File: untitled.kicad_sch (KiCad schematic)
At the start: 3 parts, among them U3 ATmega328P-P, U4 ATmega328P-P, U5 ATmega328P-P

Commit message: kicad to Jeremy
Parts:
- added Q1: NMOS, symbol Simulation_SPICE:NMOS
- added R1: 200R, symbol Device:R
- added R2: 1K, symbol Device:R
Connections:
- new net: Q1.2 (G), R1.2, R2.2
- new net GPIO_Moteur: R2.1
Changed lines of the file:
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@@
 (kicad_sch (version 20230121) (generator eeschema)
   (paper "A4")
+  (junction (at 157.48 44.45) (diameter 0) (color 0 0 0 0)
+  )
   (wire (pts (xy 163.83 86.36) (xy 170.18 86.36))
     (stroke (width 0) (type default))
   )
+  (wire (pts (xy 157.48 59.69) (xy 157.48 44.45))
+    (stroke (width 0) (type default))
+  )
+  (wire (pts (xy 157.48 44.45) (xy 161.29 44.45))
+    (stroke (width 0) (type default))
+  )
+  (wire (pts (xy 157.48 44.45) (xy 154.94 44.45))
+    (stroke (width 0) (type default))
+  )
   (wire (pts (xy 83.82 86.36) (xy 90.17 86.36))
     (stroke (width 0) (type default))
   )
+  (wire (pts (xy 158.75 59.69) (xy 157.48 59.69))
+    (stroke (width 0) (type default))
+  )
   (wire (pts (xy 83.82 88.9) (xy 90.17 88.9))
     (stroke (width 0) (type default))
@@
     (stroke (width 0) (type default))
   )
+  (wire (pts (xy 142.24 44.45) (xy 147.32 44.45))
+    (stroke (width 0) (type default))
+  )
   (wire (pts (xy 236.22 88.9) (xy 242.57 88.9))
     (stroke (width 0) (type default))
@@
     (property "Intersheetrefs" "${INTERSHEET_REFS}" (at 101.7239 88.9 0)
       (effects (font (size 1.27 1.27)) (justify left) hide)
+    )
+  )
+  (global_label "GPIO_Moteur" (shape input) (at 142.24 44.45 180) (fields_autoplaced)
+    (effects (font (size 1.27 1.27)) (justify right))
+    (property "Intersheetrefs" "${INTERSHEET_REFS}" (at 127.5414 44.45 0)
+      (effects (font (size 1.27 1.27)) (justify right) hide)
     )
   )
@@
         )
       )
+    )
+  )
+  (symbol (lib_id "Device:R") (at 151.13 44.45 90) (unit 1)
+    (in_bom yes) (on_board yes) (dnp no) (fields_autoplaced)
+    (property "Reference" "R2" (at 151.13 38.1 90)
+      (effects (font (size 1.27 1.27)))
+    )
+    (property "Value" "1K" (at 151.13 40.64 90)
+      (effects (font (size 1.27 1.27)))
+    )
+    (property "Footprint" "" (at 151.13 46.228 90)
+      (effects (font (size 1.27 1.27)) hide)
+    )
+    (property "Datasheet" "~" (at 151.13 44.45 0)
+      (effects (font (size 1.27 1.27)) hide)
+    )
+    (pin "1")
+    (pin "2")
+    (instances
+      (project "MaisonEtape1"
+        (path "/ed06f8de-d1bb-4b1a-bfe3-5df11d3a9162/0600536b-f413-4b06-98e9-b5748b5de992"
+          (reference "R2") (unit 1)
+        )
+      )
+    )
+  )
+  (symbol (lib_id "Simulation_SPICE:NMOS") (at 166.37 44.45 0) (unit 1)
+    (in_bom yes) (on_board yes) (dnp no) (fields_autoplaced)
+    (property "Reference" "Q1" (at 172.72 43.18 0)
+      (effects (font (size 1.27 1.27)) (justify left))
+    )
+    (property "Value" "NMOS" (at 172.72 45.72 0)
+      (effects (font (size 1.27 1.27)) (justify left))
+    )
+    (property "Footprint" "" (at 171.45 41.91 0)
+      (effects (font (size 1.27 1.27)) hide)
+    )
+    (property "Datasheet" "https://ngspice.sourceforge.io/docs/ngspice-manual.pdf" (at 166.37 57.15 0)
+      (effects (font (size 1.27 1.27)) hide)
+    )
+    (property "Sim.Device" "NMOS" (at 166.37 61.595 0)
+      (effects (font (size 1.27 1.27)) hide)
+    )
+    (property "Sim.Type" "VDMOS" (at 166.37 63.5 0)
+      (effects (font (size 1.27 1.27)) hide)
+    )
+    (property "Sim.Pins" "1=D 2=G 3=S" (at 166.37 59.69 0)
+      (effects (font (size 1.27 1.27)) hide)
+    )
+    (pin "1")
+    (pin "2")
+    (pin "3")
+    (instances
+      (project "MaisonEtape1"
+        (path "/ed06f8de-d1bb-4b1a-bfe3-5df11d3a9162/0600536b-f413-4b06-98e9-b5748b5de992"
+          (reference "Q1") (unit 1)
+        )
+      )
+    )
+  )
+  (symbol (lib_id "Device:R") (at 162.56 59.69 270) (unit 1)
+    (in_bom yes) (on_board yes) (dnp no) (fields_autoplaced)
+    (property "Reference" "R1" (at 162.56 53.34 90)
+      (effects (font (size 1.27 1.27)))
+    )
+    (property "Value" "200R" (at 162.56 55.88 90)
+      (effects (font (size 1.27 1.27)))
+    )
+    (property "Footprint" "" (at 162.56 57.912 90)
+      (effects (font (size 1.27 1.27)) hide)
+    )
+    (property "Datasheet" "~" (at 162.56 59.69 0)
+      (effects (font (size 1.27 1.27)) hide)
+    )
+    (pin "1")
+    (pin "2")
+    (instances
+      (project "MaisonEtape1"
+        (path "/ed06f8de-d1bb-4b1a-bfe3-5df11d3a9162/0600536b-f413-4b06-98e9-b5748b5de992"
+          (reference "R1") (unit 1)
+        )
+      )

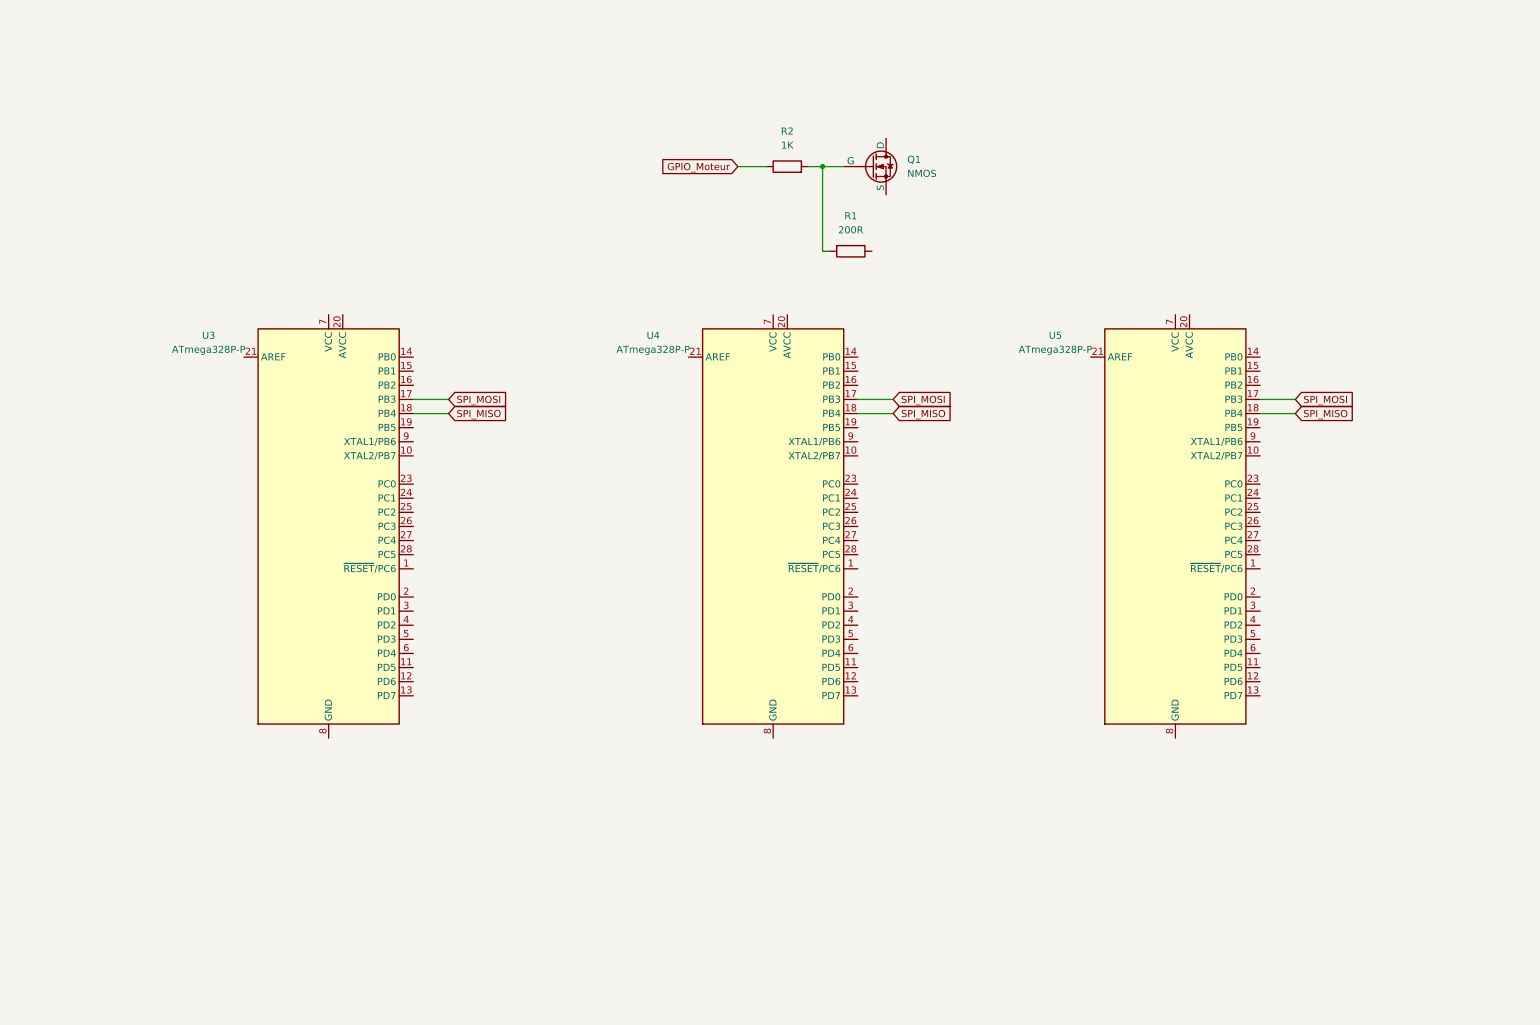
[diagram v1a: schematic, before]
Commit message: Kicad add calvier / moteur
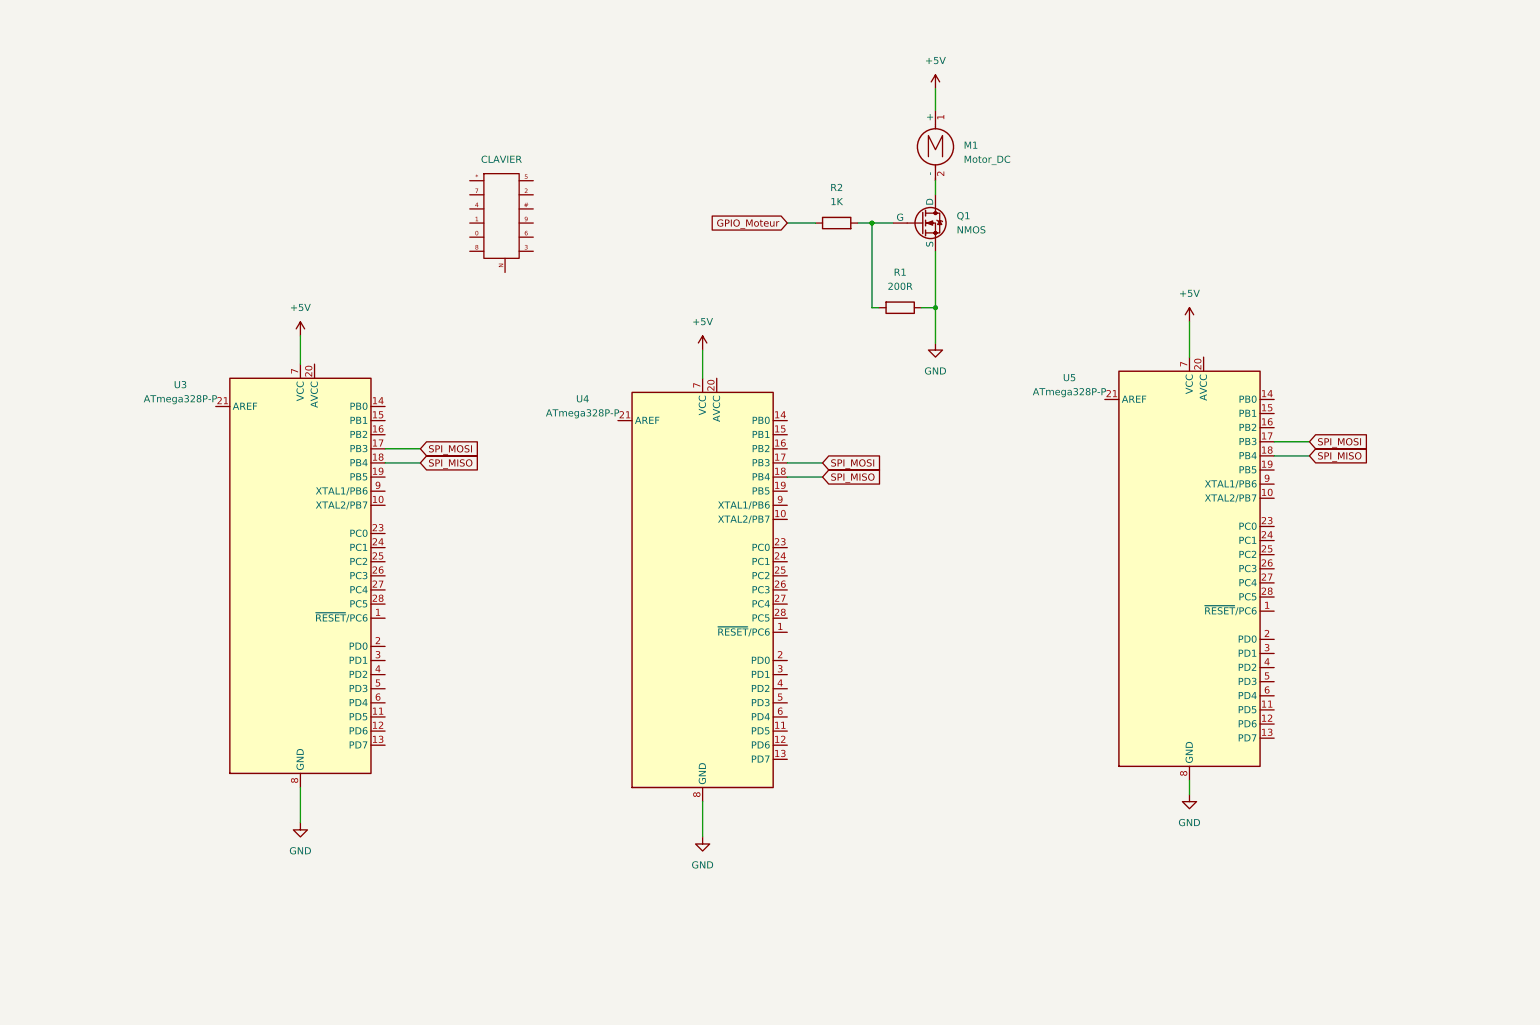
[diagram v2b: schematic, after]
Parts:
- added CLAVIER: ~, symbol New_Library:CLAV1
- added M1: Motor_DC, symbol Motor:Motor_DC
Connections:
- net GND: now reaches U3.22 (GND), U3.8 (GND)
- net GND: now also Q1.3 (S), R1.1, U4.22 (GND), U4.8 (GND), U5.22 (GND), U5.8 (GND)
- net +5V: now reaches U3.7 (VCC)
- net +5V: now also U4.7 (VCC), U5.7 (VCC), M1.1 (+)
- net at Q1.1 (D): now also M1.2 (-)
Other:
- moved on the sheet: Q1, R1, R2, U3, U4, U5

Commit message: Photon
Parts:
- removed CLAVIER: ~, symbol New_Library:CLAV1
- added CLAVIER2: ~, symbol New_Library:CLAV1

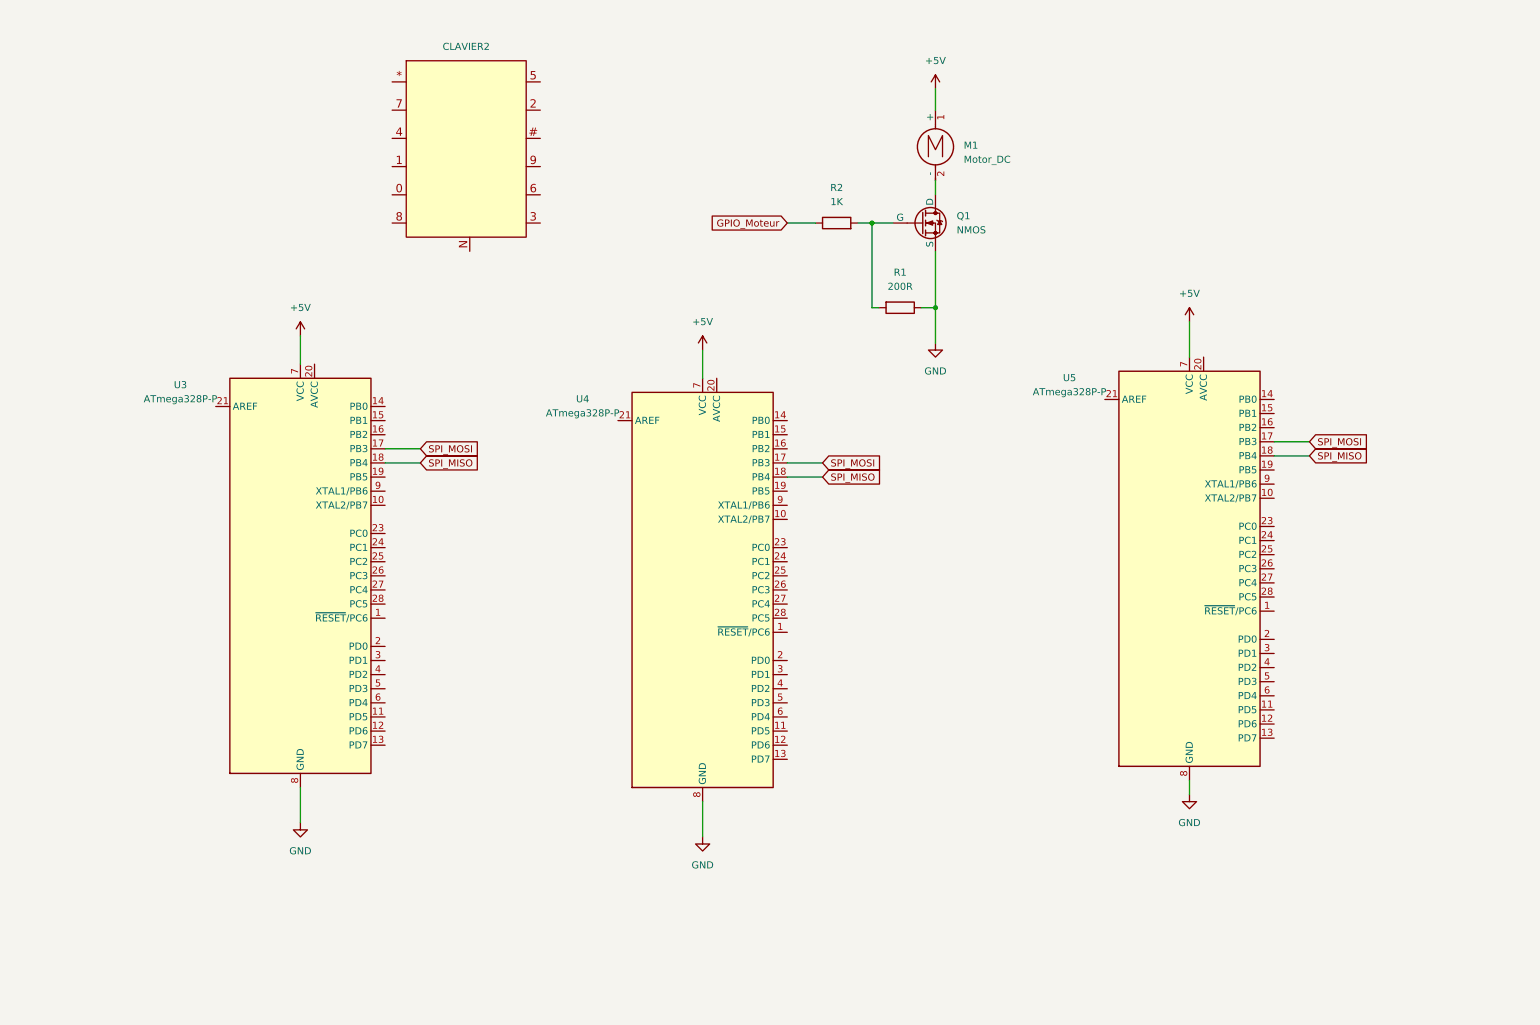
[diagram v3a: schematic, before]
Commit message: Connecteur AVR + Branchement MOSI/MISO/SCK + CS
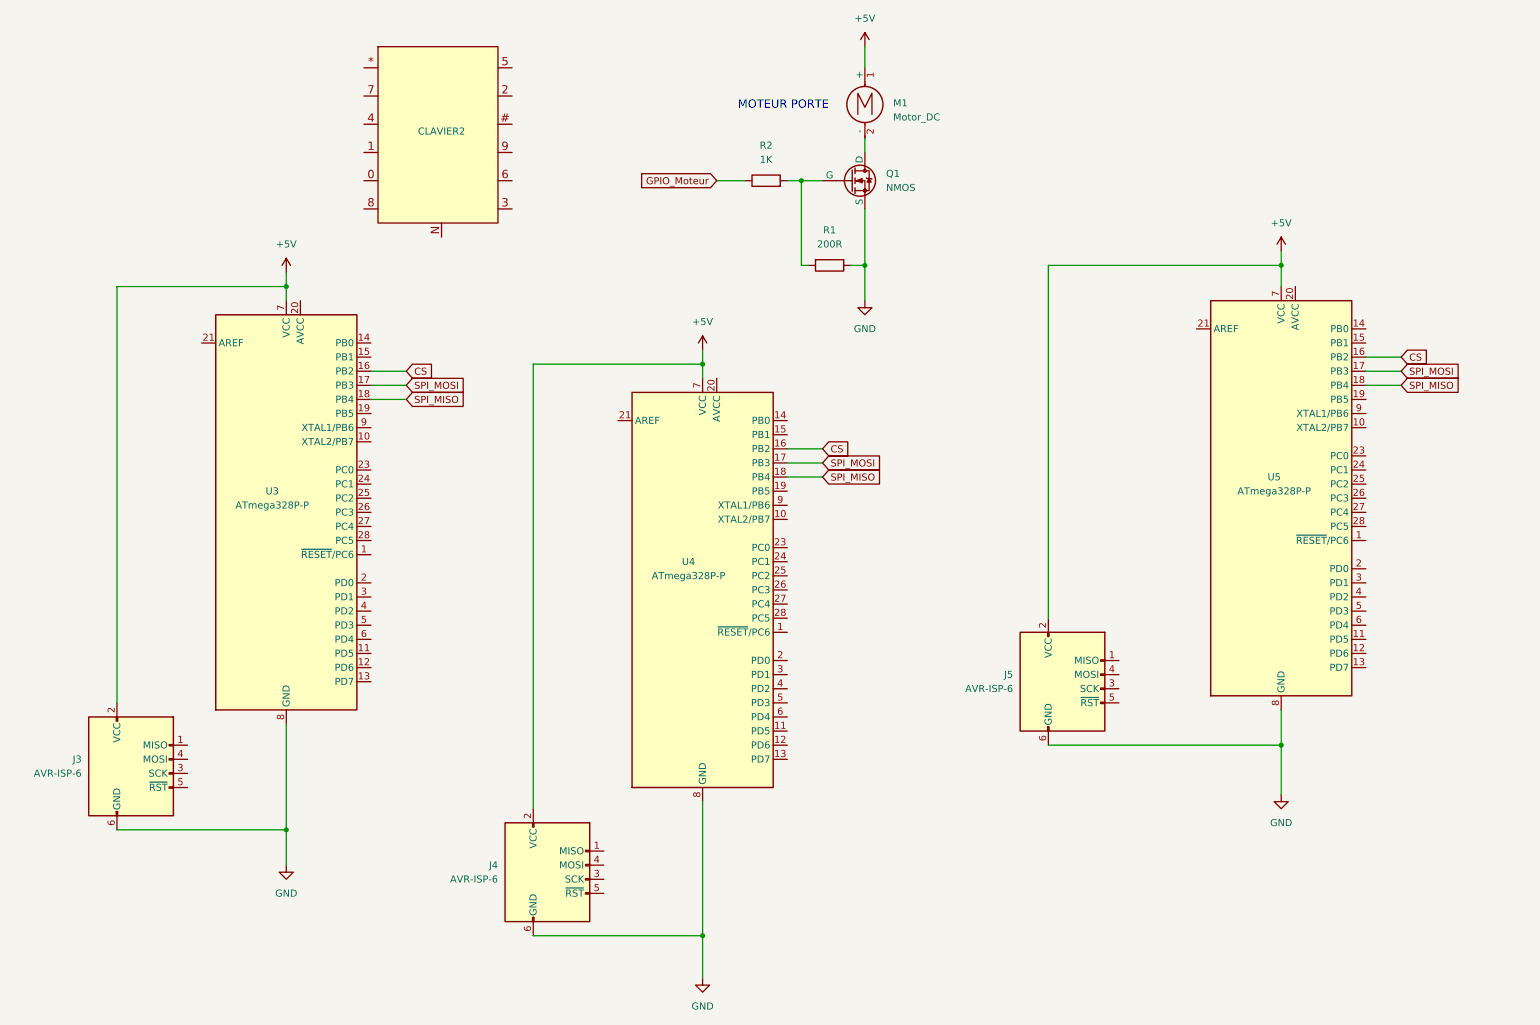
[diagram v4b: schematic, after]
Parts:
- added J3, J4, J5: AVR-ISP-6, Connector_IDC:IDC-Header_2x03_P2.54mm_Vertical, symbol Connector:AVR-ISP-6
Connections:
- net +5V: now also J3.2 (VCC), J4.2 (VCC), J5.2 (VCC)
- net GND: now also J3.6 (GND), J4.6 (GND), J5.6 (GND)
- net CS: now reaches U3.16 (PB2)
- net CS: now also U4.16 (PB2), U5.16 (PB2)
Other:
- note added: "MOTEUR PORTE"
- moved on the sheet: CLAVIER2, M1, Q1, R1, R2, U3, U5
